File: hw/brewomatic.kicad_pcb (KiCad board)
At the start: 2 copper layers, 95.2 x 70.1 mm, 36 parts, among them J1 CON_MAX31865, J10 TEST_MOC, J2 EXP1, J3 EXP2, J4 12V_IN, J5 230V_CONN, J6 HEATING_CONN, J7 PUMP_CONN, J8 12V_ALIM_CONN, J9 TEST_IN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

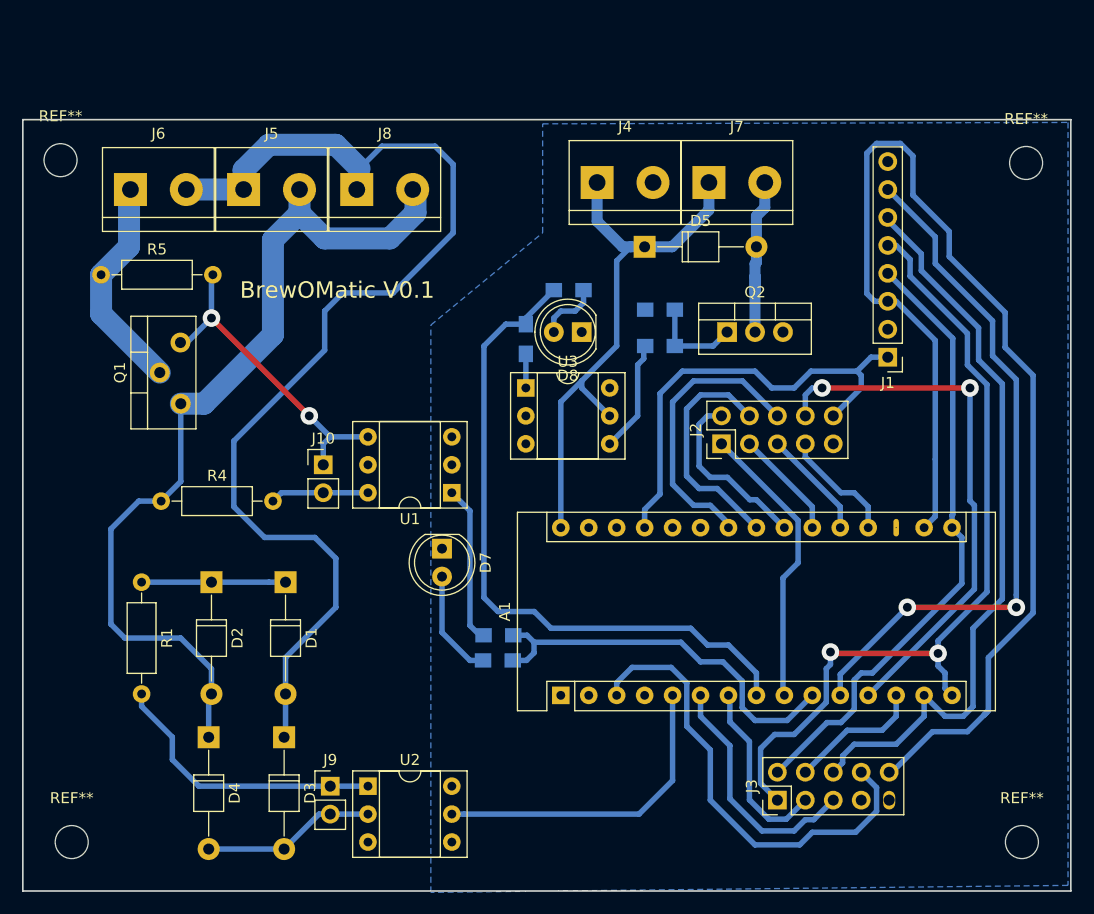
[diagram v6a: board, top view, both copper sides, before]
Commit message: Reverse triac terminal since it only works in one direction and fix various problems
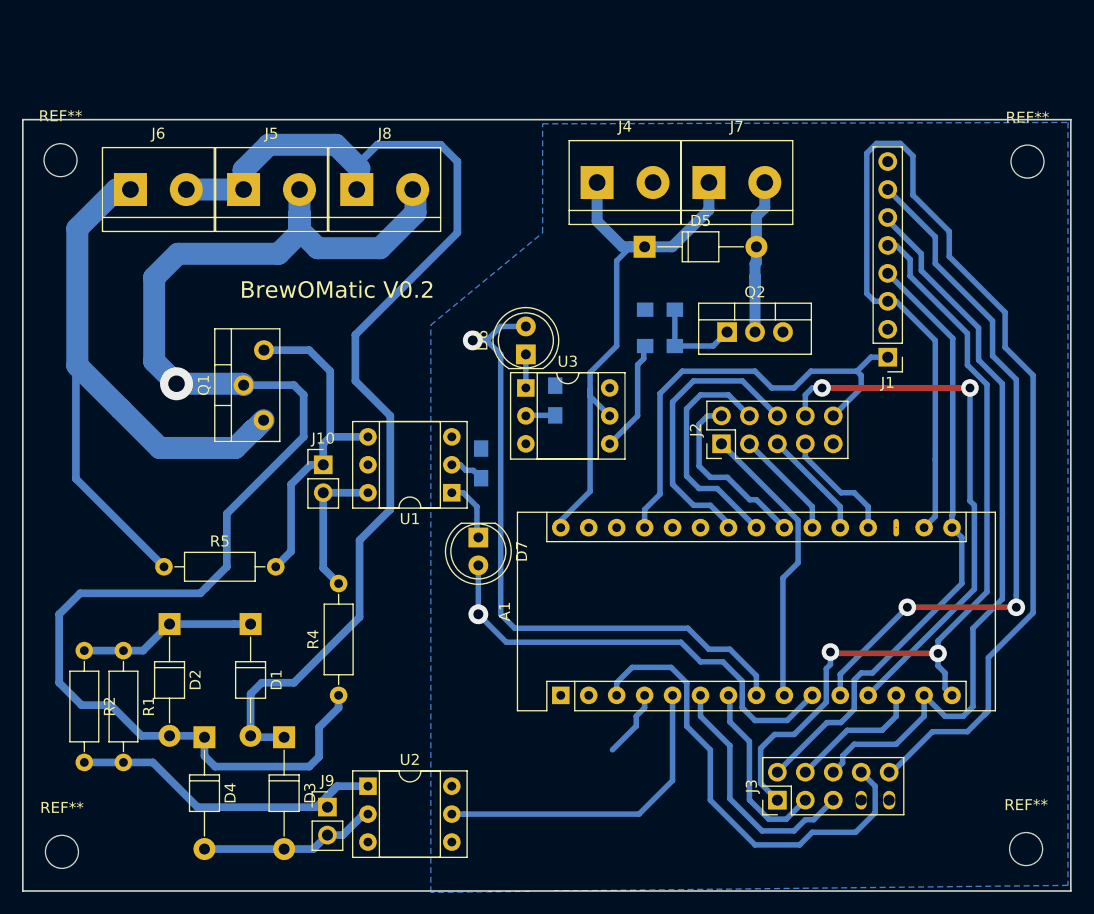
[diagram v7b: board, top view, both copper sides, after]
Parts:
- removed D8: LED, LEDs:LED_D5.0mm
- removed R10, R9: 220, Resistors_SMD:R_0805_HandSoldering
- removed the REF** at (208.0, 91.3)
- removed the REF** at (121.3, 153.0)
- removed the REF** at (207.6, 153.0)
- added D6: LED, LEDs:LED_D5.0mm, F.Cu at (162.6, 108.7)
- added R2: 45K, Resistors_THT:R_Axial_DIN0207_L6.3mm_D2.5mm_P10.16mm_Horizontal, F.Cu at (122.4, 135.6)
- added REF**: MountingHole_3mm, Mounting_Holes:MountingHole_3mm, F.Cu at (120.4, 153.9)
- added REF**: MountingHole_3mm, Mounting_Holes:MountingHole_3mm, F.Cu at (208.0, 153.7)
- added REF**: MountingHole_3mm, Mounting_Holes:MountingHole_3mm, F.Cu at (208.2, 91.2)
- J10: value TEST_MOC -> TP_MOC
- J9: value TEST_IN -> TEST_ZERO
- moved R5 27.2 mm to (129.7, 128.0)
- moved R4 23.9 mm to (145.5, 139.7), turned to 90 degrees
- moved R3 15.7 mm to (158.5, 118.6), turned to 270 degrees
- moved Q1 7.71 mm to (136.9, 114.0)
- moved R1 6.44 mm to (126.0, 135.6)
- moved R6 6.19 mm to (165.2, 112.9), turned to 270 degrees
- moved D2 5.39 mm to (130.2, 133.2)
- moved D1 4.96 mm to (137.5, 133.2)
- moved D7 3.45 mm to (158.2, 125.3)
- moved J9 1.92 mm to (144.5, 149.9)
- moved D4 0.38 mm to (133.3, 143.5)
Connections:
- A1 pad 1: (no net) -> Net-(A1-Pad1)
- A1 pad 18: (no net) -> Net-(A1-Pad18)
- A1 pad 2: (no net) -> Net-(A1-Pad2)
- A1 pad 25: (no net) -> Net-(A1-Pad25)
- A1 pad 26: (no net) -> Net-(A1-Pad26)
- A1 pad 28: (no net) -> Net-(A1-Pad28)
- D7 pad 1: GND -> Net-(D7-Pad1)
- D7 pad 2: Net-(D7-Pad2) -> /TRIAC_CTRL
- J1 pad 8: (no net) -> /TEMP_DRDY
- J3 pad 7: (no net) -> Net-(J3-Pad7)
- Q1 pad 1: LINE -> /HEATING_LINE
- Q1 pad 2: /HEATING_LINE -> LINE
- R3 pad 1: Net-(R3-Pad1) -> GND
- R3 pad 2: /TRIAC_CTRL -> Net-(R3-Pad2)
- R6 pad 1: Net-(R6-Pad1) -> GND
- R6 pad 2: /PUMP_CTRL -> Net-(R6-Pad2)
- U1 pad 1: Net-(R3-Pad1) -> Net-(D7-Pad1)
- U1 pad 2: GND -> Net-(R3-Pad2)
- U1 pad 3: (no net) -> Net-(U1-Pad3)
- U1 pad 5: (no net) -> Net-(U1-Pad5)
- U2 pad 3: (no net) -> Net-(U2-Pad3)
- U2 pad 6: (no net) -> Net-(U2-Pad6)
- U3 pad 1: Net-(R6-Pad1) -> Net-(D6-Pad1)
- U3 pad 2: GND -> Net-(R6-Pad2)
- U3 pad 3: (no net) -> Net-(U3-Pad3)
- U3 pad 6: (no net) -> Net-(U3-Pad6)
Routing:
- net LINE: track 80.8 -> 134.1 mm, vias 0 -> 1
- net /HEATING_LINE: track 20.0 -> 61.7 mm
- net Net-(R3-Pad1): track 14.4 -> 0.00 mm
- net Net-(D7-Pad2): track 9.86 -> 0.00 mm
- net GND: track 0.00 -> 6.16 mm
- net Net-(D7-Pad1): track 0.00 -> 5.73 mm
- net Net-(D8-Pad2): track 5.70 -> 0.00 mm
- net /TRIAC_CTRL: track 35.9 -> 41.2 mm, vias 0 -> 1
- net Net-(J9-Pad1): track 25.9 -> 30.5 mm
- net Net-(J10-Pad2): track 8.95 -> 12.9 mm
- net Net-(R3-Pad2): track 0.00 -> 3.17 mm
- net /PUMP_CTRL: track 61.3 -> 58.1 mm, vias 0 -> 1
- net Net-(R6-Pad1): track 3.09 -> 0.00 mm
- net Net-(D6-Pad1): track 0.00 -> 3.05 mm
- net Net-(R6-Pad2): track 0.00 -> 2.69 mm
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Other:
- board text added: "BrewOMatic V0.2"
- board text removed: "BrewOMatic V0.1"

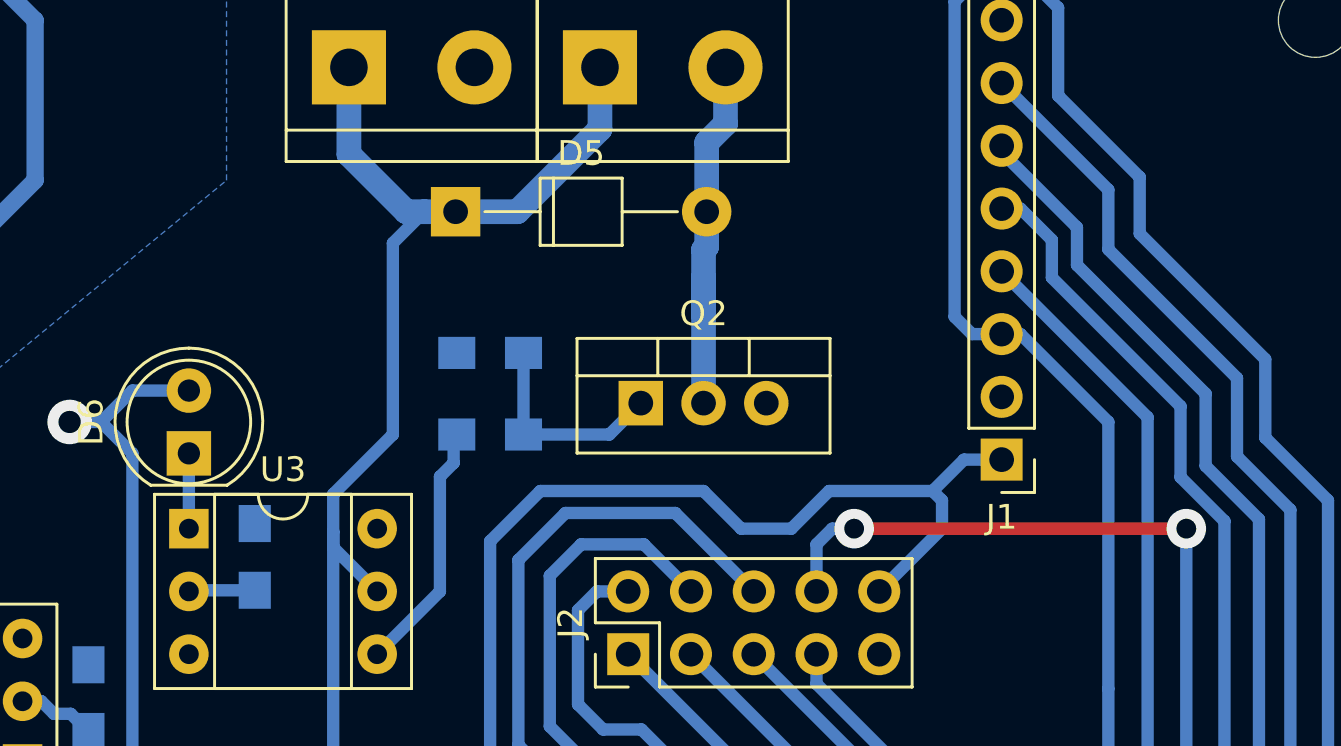
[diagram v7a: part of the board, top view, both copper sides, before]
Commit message: Add 12V fan plug
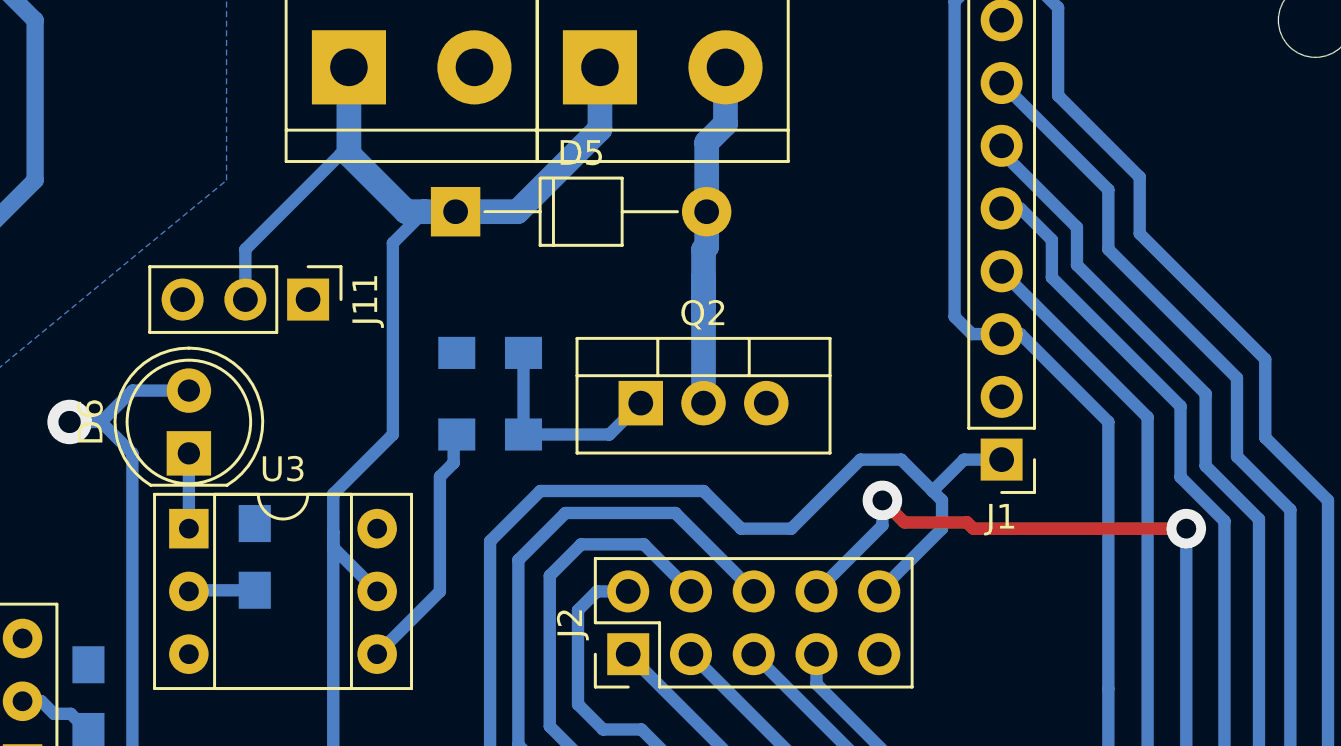
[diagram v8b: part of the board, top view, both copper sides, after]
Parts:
- added J11: FAN, Pin_Headers:Pin_Header_Straight_1x03_Pitch2.54mm, F.Cu at (167.4, 102.5)
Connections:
- J1 pad 2: GND -> Net-(J1-Pad2)
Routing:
- net +12V: track 49.8 -> 57.6 mm
- net +5V: track 41.4 -> 42.4 mm
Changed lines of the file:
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@@
 (kicad_pcb (version 4) (host pcbnew 4.0.7+dfsg1-1)
   (general
-    (links 74)
-    (no_connects 0)
+    (links 75)
+    (no_connects 1)
     (area 112.854714 71.928929 227.56 158.999)
     (thickness 1.6)
     (drawings 7)
-    (tracks 372)
+    (tracks 378)
     (zones 0)
-    (modules 35)
-    (nets 53)
+    (modules 36)
+    (nets 55)
   )
   (page A4)
@@
   )
   (setup
-    (last_trace_width 0.7)
+    (last_trace_width 0.5)
     (user_trace_width 0.7)
     (user_trace_width 1)
@@
   (net 51 "Net-(R3-Pad2)")
   (net 52 "Net-(R6-Pad2)")
+  (net 53 "Net-(J1-Pad2)")
+  (net 54 "Net-(J11-Pad1)")
   (net_class Default "Ceci est la Netclass par défaut"
     (clearance 0.2)
@@
     (add_net "Net-(D6-Pad1)")
     (add_net "Net-(D7-Pad1)")
+    (add_net "Net-(J1-Pad2)")
     (add_net "Net-(J10-Pad1)")
     (add_net "Net-(J10-Pad2)")
+    (add_net "Net-(J11-Pad1)")
     (add_net "Net-(J3-Pad7)")
     (add_net "Net-(J9-Pad1)")
@@
       (net 14 +5V))
     (pad 2 thru_hole oval (at 0 2.54 180) (size 1.7 1.7) (drill 1) (layers *.Cu *.Mask)
-      (net 3 GND))
+      (net 53 "Net-(J1-Pad2)"))
     (pad 3 thru_hole oval (at 0 5.08 180) (size 1.7 1.7) (drill 1) (layers *.Cu *.Mask)
       (net 1 +3V3))
@@
       (at (xyz 0.1 0 0))
       (scale (xyz 0.393701 0.393701 0.393701))
+      (rotate (xyz 0 0 0))
+    )
+  )
+  (module Pin_Headers:Pin_Header_Straight_1x03_Pitch2.54mm (layer F.Cu)
+    (at 167.386 102.489 270)
+    (descr "Through hole straight pin header, 1x03, 2.54mm pitch, single row")
+    (tags "Through hole pin header THT 1x03 2.54mm single row")
+    (fp_text reference J11 (at 0 -2.33 270) (layer F.SilkS)
+      (effects (font (size 1 1) (thickness 0.15)))
+    )
+    (fp_text value FAN (at 0 7.41 270) (layer F.Fab)
+      (effects (font (size 1 1) (thickness 0.15)))
+    )
+    (fp_line (start -0.635 -1.27) (end 1.27 -1.27) (layer F.Fab) (width 0.1))
+    (fp_line (start 1.27 -1.27) (end 1.27 6.35) (layer F.Fab) (width 0.1))
+    (fp_line (start 1.27 6.35) (end -1.27 6.35) (layer F.Fab) (width 0.1))
+    (fp_line (start -1.27 6.35) (end -1.27 -0.635) (layer F.Fab) (width 0.1))
+    (fp_line (start -1.27 -0.635) (end -0.635 -1.27) (layer F.Fab) (width 0.1))
+    (fp_line (start -1.33 6.41) (end 1.33 6.41) (layer F.SilkS) (width 0.12))
+    (fp_line (start -1.33 1.27) (end -1.33 6.41) (layer F.SilkS) (width 0.12))
+    (fp_line (start 1.33 1.27) (end 1.33 6.41) (layer F.SilkS) (width 0.12))
+    (fp_line (start -1.33 1.27) (end 1.33 1.27) (layer F.SilkS) (width 0.12))
+    (fp_line (start -1.33 0) (end -1.33 -1.33) (layer F.SilkS) (width 0.12))
+    (fp_line (start -1.33 -1.33) (end 0 -1.33) (layer F.SilkS) (width 0.12))
+    (fp_line (start -1.8 -1.8) (end -1.8 6.85) (layer F.CrtYd) (width 0.05))
+    (fp_line (start -1.8 6.85) (end 1.8 6.85) (layer F.CrtYd) (width 0.05))
+    (fp_line (start 1.8 6.85) (end 1.8 -1.8) (layer F.CrtYd) (width 0.05))
+    (fp_line (start 1.8 -1.8) (end -1.8 -1.8) (layer F.CrtYd) (width 0.05))
+    (fp_text user %R (at 0 2.54 360) (layer F.Fab)
+      (effects (font (size 1 1) (thickness 0.15)))
+    )
+    (pad 1 thru_hole rect (at 0 0 270) (size 1.7 1.7) (drill 1) (layers *.Cu *.Mask)
+      (net 54 "Net-(J11-Pad1)"))
+    (pad 2 thru_hole oval (at 0 2.54 270) (size 1.7 1.7) (drill 1) (layers *.Cu *.Mask)
+      (net 19 +12V))
+    (pad 3 thru_hole oval (at 0 5.08 270) (size 1.7 1.7) (drill 1) (layers *.Cu *.Mask)
+      (net 3 GND))
+    (model ${KISYS3DMOD}/Pin_Headers.3dshapes/Pin_Header_Straight_1x03_Pitch2.54mm.wrl
+      (at (xyz 0 0 0))
+      (scale (xyz 1 1 1))
       (rotate (xyz 0 0 0))
     )
@@
   (segment (start 181.102 142.113) (end 181.102 139.827) (width 0.5) (layer B.Cu) (net 9))
   (segment (start 181.102 139.827) (end 180.975 139.7) (width 0.5) (layer B.Cu) (net 9))
+  (segment (start 202.92601 111.76) (end 194.31 111.76) (width 0.5) (layer F.Cu) (net 10))
+  (segment (start 194.31 111.76) (end 194.056 111.506) (width 0.5) (layer F.Cu) (net 10))
+  (segment (start 194.056 111.506) (end 191.516 111.506) (width 0.5) (layer F.Cu) (net 10))
+  (segment (start 191.516 111.506) (end 190.627 110.617) (width 0.5) (layer F.Cu) (net 10))
+  (segment (start 187.96 114.3) (end 190.627 111.633) (width 0.5) (layer B.Cu) (net 10))
+  (segment (start 190.627 111.633) (end 190.627 110.617) (width 0.5) (layer B.Cu) (net 10))
+  (via (at 190.627 110.617) (size 1.6) (drill 0.8) (layers F.Cu B.Cu) (net 10))
   (segment (start 193.675 139.7) (end 203.327 130.048) (width 0.5) (layer B.Cu) (net 10))
   (segment (start 203.327 130.048) (end 203.327 122.428) (width 0.5) (layer B.Cu) (net 10))
@@
   (segment (start 203.327 122.428) (end 202.92601 122.02701) (width 0.5) (layer B.Cu) (net 10))
   (via (at 202.92601 111.76) (size 1.6) (drill 0.8) (layers F.Cu B.Cu) (net 10))
-  (segment (start 189.484 111.76) (end 202.92601 111.76) (width 0.5) (layer F.Cu) (net 10))
-  (segment (start 189.484 111.76) (end 188.595 111.76) (width 0.5) (layer B.Cu) (net 10))
-  (segment (start 188.595 111.76) (end 187.96 112.395002) (width 0.5) (layer B.Cu) (net 10))
-  (segment (start 187.96 112.395002) (end 187.96 114.3) (width 0.5) (layer B.Cu) (net 10))
-  (via (at 189.484 111.76) (size 1.6) (drill 0.8) (layers F.Cu B.Cu) (net 10))
   (segment (start 183.515 124.46) (end 179.959 120.904) (width 0.5) (layer B.Cu) (net 11))
   (segment (start 179.959 120.904) (end 178.308 120.904) (width 0.5) (layer B.Cu) (net 11))
@@
   (segment (start 182.225001 138.410001) (end 182.225001 140.823001) (width 0.5) (layer B.Cu) (net 13))
   (segment (start 186.309 141.986) (end 188.595 139.7) (width 0.5) (layer B.Cu) (net 13))
+  (segment (start 173.355 124.46) (end 173.355 122.809) (width 0.5) (layer B.Cu) (net 14))
+  (segment (start 176.784 110.236) (end 183.388 110.236) (width 0.5) (layer B.Cu) (net 14))
+  (segment (start 173.355 122.809) (end 174.752 121.412) (width 0.5) (layer B.Cu) (net 14))
+  (segment (start 174.752 121.412) (end 174.752 112.268) (width 0.5) (layer B.Cu) (net 14))
+  (segment (start 174.752 112.268) (end 176.784 110.236) (width 0.5) (layer B.Cu) (net 14))
+  (segment (start 183.388 110.236) (end 184.912 111.76) (width 0.5) (layer B.Cu) (net 14))
+  (segment (start 184.912 111.76) (end 186.944 111.76) (width 0.5) (layer B.Cu) (net 14))
+  (segment (start 186.944 111.76) (end 189.738 108.966) (width 0.5) (layer B.Cu) (net 14))
+  (segment (start 189.738 108.966) (end 191.389 108.966) (width 0.5) (layer B.Cu) (net 14))
+  (segment (start 191.389 108.966) (end 192.659 110.236) (width 0.5) (layer B.Cu) (net 14))
   (segment (start 192.659 110.236) (end 193.929 108.966) (width 0.5) (layer B.Cu) (net 14))
   (segment (start 193.929 108.966) (end 195.453 108.966) (width 0.5) (layer B.Cu) (net 14))
   (segment (start 193.04 111.76) (end 193.04 110.617) (width 0.5) (layer B.Cu) (net 14))
   (segment (start 193.04 110.617) (end 192.659 110.236) (width 0.5) (layer B.Cu) (net 14))
-  (segment (start 173.355 124.46) (end 173.355 122.809) (width 0.5) (layer B.Cu) (net 14))
-  (segment (start 173.355 122.809) (end 174.752 121.412) (width 0.5) (layer B.Cu) (net 14))
-  (segment (start 174.752 121.412) (end 174.752 112.268) (width 0.5) (layer B.Cu) (net 14))
-  (segment (start 174.752 112.268) (end 176.784 110.236) (width 0.5) (layer B.Cu) (net 14))
-  (segment (start 176.784 110.236) (end 183.388 110.236) (width 0.5) (layer B.Cu) (net 14))
-  (segment (start 183.388 110.236) (end 184.912 111.76) (width 0.5) (layer B.Cu) (net 14))
-  (segment (start 184.912 111.76) (end 186.944 111.76) (width 0.5) (layer B.Cu) (net 14))
-  (segment (start 186.944 111.76) (end 188.468 110.236) (width 0.5) (layer B.Cu) (net 14))
-  (segment (start 188.468 110.236) (end 192.659 110.236) (width 0.5) (layer B.Cu) (net 14))
   (segment (start 193.04 111.76) (end 190.5 114.3) (width 0.5) (layer B.Cu) (net 14))
   (segment (start 188.595 122.555) (end 188.595 124.46) (width 0.5) (layer B.Cu) (net 15))
@@
   (segment (start 191.349999 145.835001) (end 191.349999 145.200001) (width 0.5) (layer B.Cu) (net 18))
   (segment (start 198.755 141.605) (end 198.755 139.7) (width 0.5) (layer B.Cu) (net 18))
+  (segment (start 169.037 96.615) (end 168.688 96.615) (width 0.5) (layer B.Cu) (net 19))
+  (segment (start 168.688 96.615) (end 164.846 100.457) (width 0.5) (layer B.Cu) (net 19))
+  (segment (start 164.846 100.457) (end 164.846 102.489) (width 0.5) (layer B.Cu) (net 19))
   (segment (start 165.735 124.46) (end 165.735 123.825) (width 0.5) (layer B.Cu) (net 19))
   (segment (start 165.735 123.825) (end 168.402 121.158) (width 0.5) (layer B.Cu) (net 19))
